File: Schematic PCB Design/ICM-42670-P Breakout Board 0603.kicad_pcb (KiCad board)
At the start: 2 copper layers, 19.5 x 26.5 mm, 16 parts, among them J2 Conn_01x09_Pin, U1 ICM-42670-P, U3 MCP1700x-330xxTT

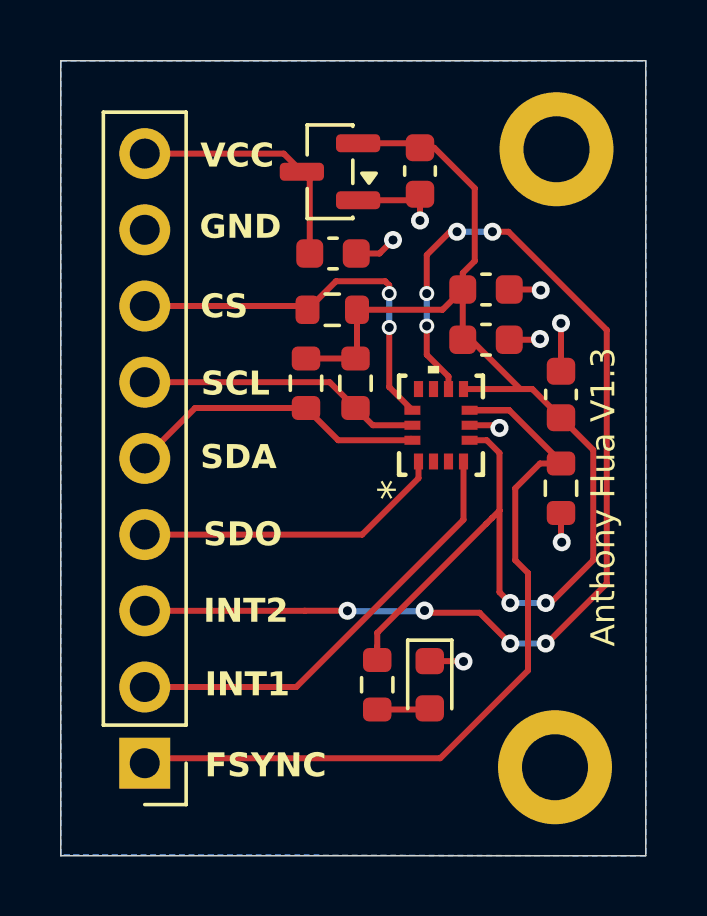
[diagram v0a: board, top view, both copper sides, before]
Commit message: Removed Via from 3V3 To reduce inductance
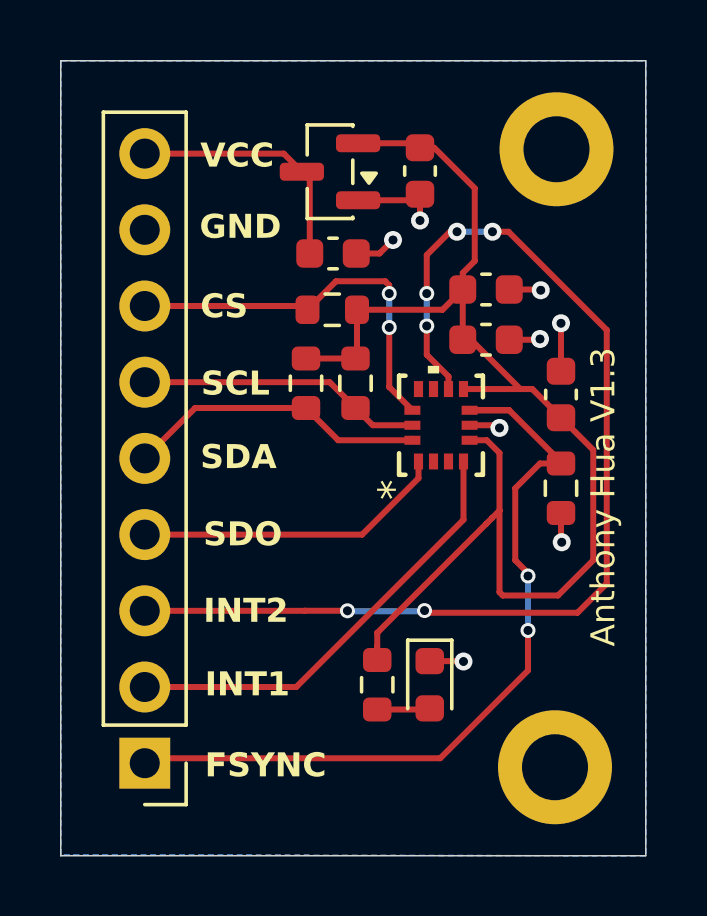
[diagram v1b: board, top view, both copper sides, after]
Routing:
- net /INT2: track 37.6 -> 36.8 mm, vias 8 -> 6
- net /3V3_Clean: track 44.8 -> 44.6 mm, vias 2 -> 0
- net /FSYNC: vias 0 -> 2

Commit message: Remove My name Put sleepypandas
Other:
- board text removed: "Anthony Hua V1.3"
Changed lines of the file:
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@@
 		(layer "Edge.Cuts")
-	)
-	(gr_text "Anthony Hua V1.3"
-		(at 74.05 42.525 90)
-		(layer "F.SilkS")
-		(effects
-			(font
-				(size 0.8 0.8)
-				(thickness 0.1)
-			)
-			(justify left bottom)
-		)
 	)
 	(gr_text "GND"
